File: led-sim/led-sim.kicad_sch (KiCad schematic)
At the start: 6 parts, among them Q1 MMBT3904

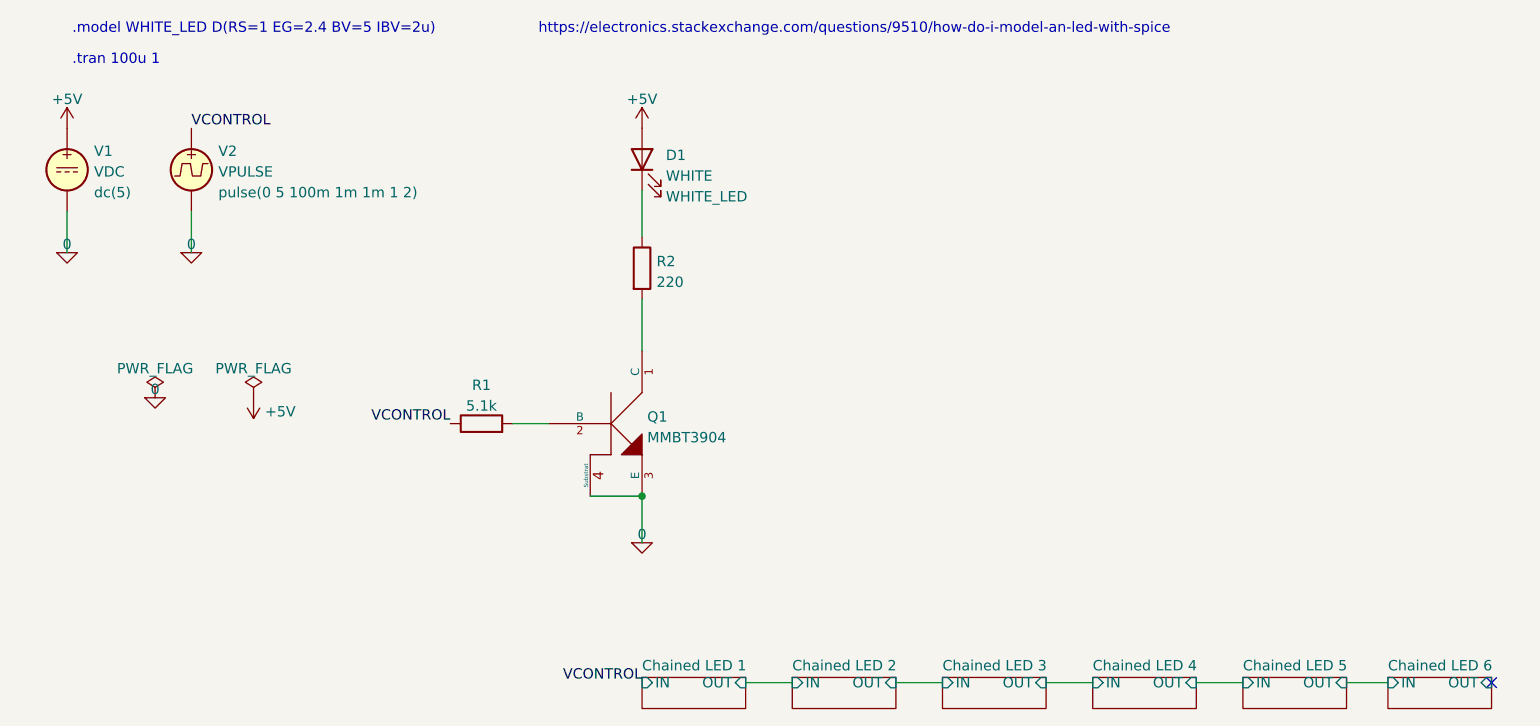
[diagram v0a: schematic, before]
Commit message: sim for LED timings with gate in between
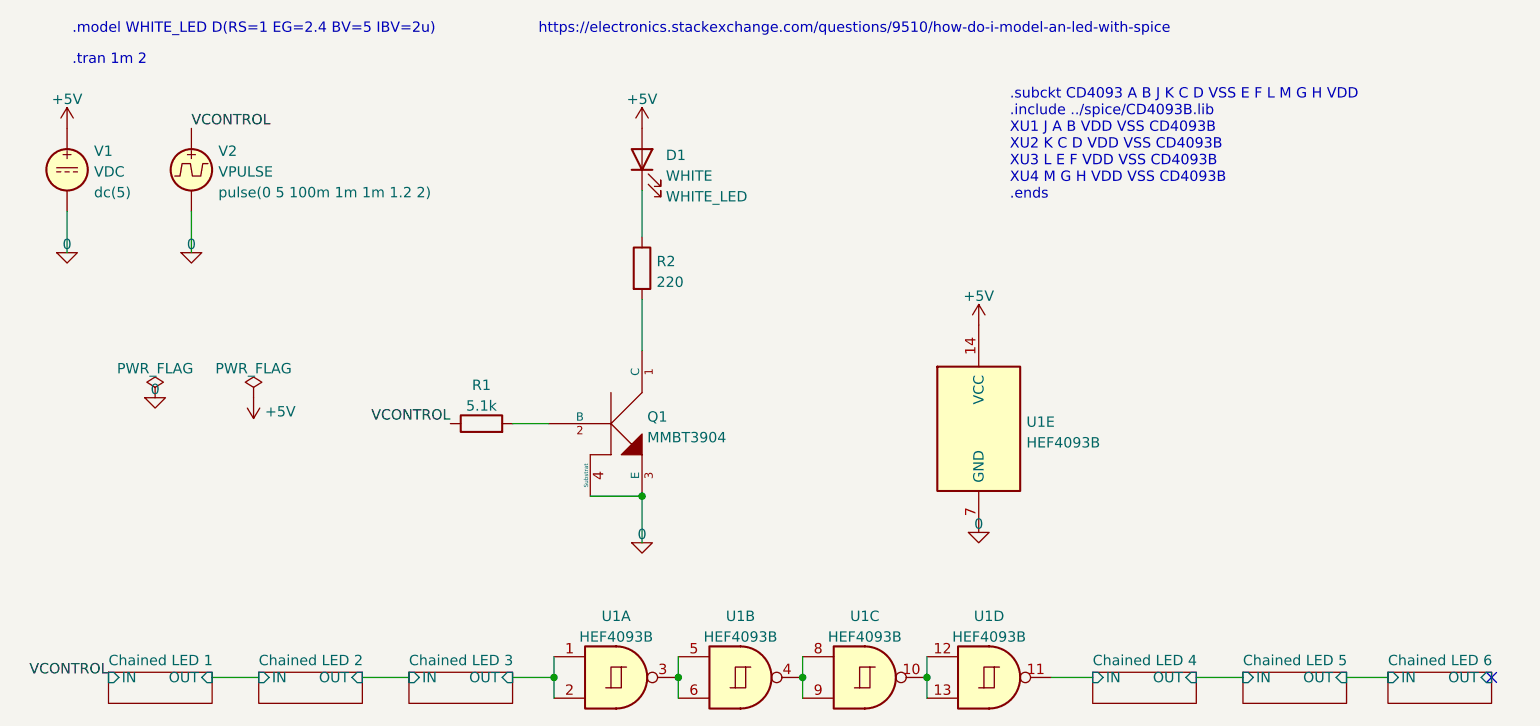
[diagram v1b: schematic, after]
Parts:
- added U1: HEF4093B, symbol 4xxx:HEF4093B
- V2: Spice_Model pulse(0 5 100m 1m 1m 1 2) -> pulse(0 5 100m 1m 1m 1.2 2)
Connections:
- net +5V: now also U1.14 (VCC)
- net 0: now also U1.7 (GND)
- net Chained LED 3/OUT: now also U1.1, U1.2
- new net: U1.10, U1.12, U1.13
- new net: U1.4, U1.8, U1.9
- new net: U1.3, U1.5, U1.6
- new net Chained LED 4/IN: U1.11
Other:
- note added: ".subckt CD4093 A B J K C D VSS E F L M G H VDD .include ../spice/CD4093B.lib XU1 J A B VDD VSS CD4093B XU2 K C D VDD VSS CD4093B XU3 L E F VDD VSS CD4093B XU4 M G H VDD VSS CD4093B .ends"
- note added: ".tran 1m 2"
- note removed: ".tran 100u 1"
